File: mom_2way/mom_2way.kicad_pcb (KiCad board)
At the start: 2 copper layers, 15 x 17 mm, 9 parts, among them J1 I/O connector

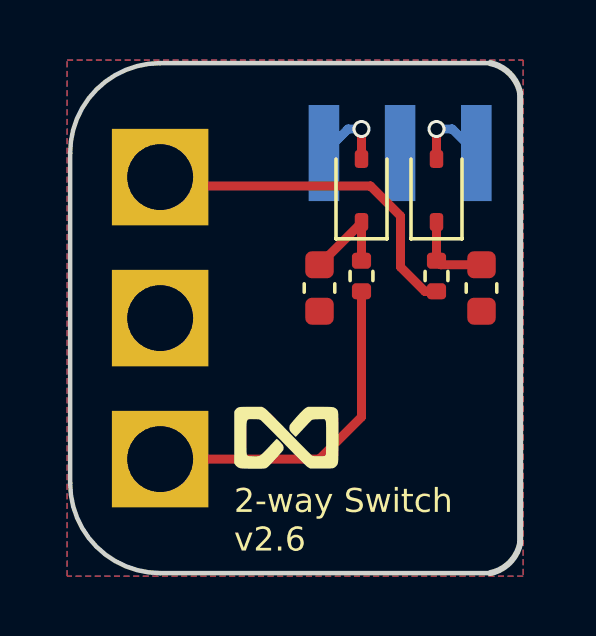
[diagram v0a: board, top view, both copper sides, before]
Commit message: 2-Way Switch refinements
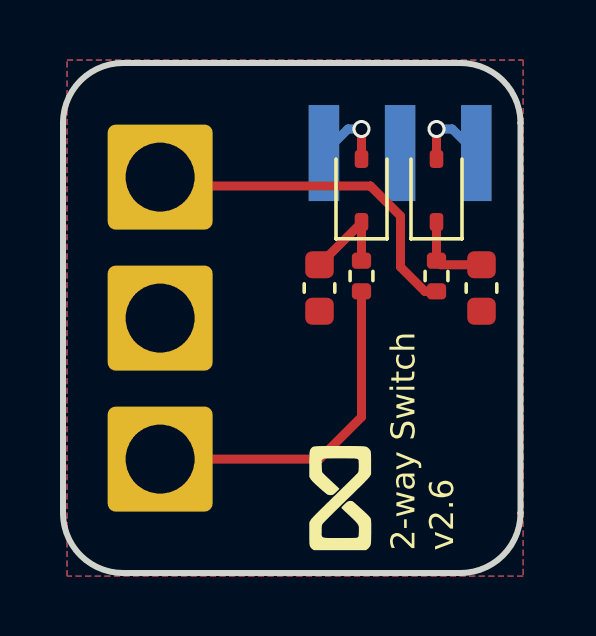
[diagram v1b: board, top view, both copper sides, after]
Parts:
- moved G*** 2.69 mm to (150.0, 111.0), turned to 90 degrees
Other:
- board size 15 x 17 mm -> 15.2 x 17 mm
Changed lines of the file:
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@@
 		(sheetname "/")
 		(sheetfile "mom_2way.kicad_sch")
-		(pad "1" thru_hole rect
+		(pad "1" thru_hole roundrect
 			(at -4.7 0 270)
-			(size 3.216 3.216)
-			(drill 2.2)
+			(size 3.5 3.5)
+			(drill 2.3)
 			(layers "*.Cu" "*.Mask")
 			(remove_unused_layers no)
+			(roundrect_rratio 0.07692307692)
 			(net 5 "Net-(S1-O)")
 			(pinfunction "O")
@@
 			(thermal_bridge_angle 0)
 		)
-		(pad "2" thru_hole rect
+		(pad "2" thru_hole roundrect
 			(at 0 0 270)
-			(size 3.216 3.216)
-			(drill 2.2)
+			(size 3.5 3.5)
+			(drill 2.3)
 			(layers "*.Cu" "*.Mask")
 			(remove_unused_layers no)
+			(roundrect_rratio 0.07692307692)
 			(net 1 "GND")
 			(pinfunction "P")
@@
 			(thermal_bridge_angle 0)
 		)
-		(pad "3" thru_hole rect
+		(pad "3" thru_hole roundrect
 			(at 4.7 0 270)
-			(size 3.216 3.216)
-			(drill 2.2)
+			(size 3.5 3.5)
+			(drill 2.3)
 			(layers "*.Cu" "*.Mask")
 			(remove_unused_layers no)
+			(roundrect_rratio 0.07692307692)
 			(net 4 "Net-(S1-S)")
 			(pinfunction "S")
@@
 		)
 		(embedded_fonts no)
+		(model "${CYCFI_COMMON}/step_files/141_100SPxT1B1M1xE.stp"
+			(offset
+				(xyz 0 0 7)
+			)
+			(scale
+				(xyz 1 1 1)
+			)
+			(rotate
+				(xyz -0 -0 -0)
+			)
+		)
 	)
 	(footprint "cycfi_library:infinity_logo_4mm"
 		(layer "F.Cu")
-		(at 148.2 109)
+		(at 150 111 90)
 		(property "Reference" "G***"
-			(at 0 0 0)
+			(at 0 0 90)
 			(layer "F.SilkS")
 			(hide yes)
@@
 		)
 		(property "Value" "LOGO"
-			(at 0.75 0 0)
+			(at 0.75 0 90)
 			(layer "F.SilkS")
 			(hide yes)
@@
 		)
 		(property "Datasheet" ""
-			(at 0 0 0)
+			(at 0 0 90)
 			(layer "F.Fab")
 			(hide yes)
@@
 		)
 		(property "Description" ""
-			(at 0 0 0)
+			(at 0 0 90)
 			(layer "F.Fab")
 			(hide yes)
@@
 	)
 	(gr_line
-		(start 154.9878 96.503599)
-		(end 143.9878 96.503599)
-		(stroke
-			(width 0.15)
-			(type solid)
+		(start 140.75 111.5)
+		(end 140.75 98.5)
+		(stroke
+			(width 0.2)
+			(type default)
 		)
 		(layer "Edge.Cuts")
 	)
 	(gr_line
-		(start 143.9878 113.503599)
-		(end 154.9878 113.503599)
-		(stroke
-			(width 0.15)
-			(type solid)
+		(start 156 98.5)
+		(end 156 111.5)
+		(stroke
+			(width 0.2)
+			(type default)
+		)
+		(layer "Edge.Cuts")
+	)
+	(gr_arc
+		(start 154 96.5)
+		(mid 155.414214 97.085786)
+		(end 156 98.5)
+		(stroke
+			(width 0.2)
+			(type default)
 		)
 		(layer "Edge.Cuts")
 	)
 	(gr_line
-		(start 155.9878 97.503599)
-		(end 155.9878 112.503599)
-		(stroke
-			(width 0.2032)
-			(type solid)
+		(start 142.75 96.5)
+		(end 154 96.5)
+		(stroke
+			(width 0.2)
+			(type default)
+		)
+		(layer "Edge.Cuts")
+	)
+	(gr_line
+		(start 154 113.5)
+		(end 142.75 113.5)
+		(stroke
+			(width 0.2)
+			(type default)
 		)
 		(layer "Edge.Cuts")
 	)
 	(gr_arc
-		(start 143.9878 113.503599)
-		(mid 141.86648 112.624919)
-		(end 140.9878 110.503599)
-		(stroke
-			(width 0.15)
-			(type solid)
+		(start 140.75 98.5)
+		(mid 141.335786 97.085786)
+		(end 142.75 96.5)
+		(stroke
+			(width 0.2)
+			(type default)
 		)
 		(layer "Edge.Cuts")
 	)
 	(gr_arc
-		(start 140.9878 99.503599)
-		(mid 141.86648 97.382279)
-		(end 143.9878 96.503599)
-		(stroke
-			(width 0.15)
-			(type solid)
+		(start 156 111.5)
+		(mid 155.414214 112.914214)
+		(end 154 113.5)
+		(stroke
+			(width 0.2)
+			(type default)
 		)
 		(layer "Edge.Cuts")
 	)
 	(gr_arc
-		(start 155.9878 112.503599)
-		(mid 155.639188 113.154988)
-		(end 154.987799 113.5036)
-		(stroke
-			(width 0.2032)
-			(type solid)
-		)
-		(layer "Edge.Cuts")
-	)
-	(gr_arc
-		(start 154.9878 96.503599)
-		(mid 155.639188 96.852212)
-		(end 155.9878 97.503601)
-		(stroke
-			(width 0.2032)
-			(type solid)
-		)
-		(layer "Edge.Cuts")
-	)
-	(gr_line
-		(start 140.9878 99.503599)
-		(end 140.9878 110.503599)
-		(stroke
-			(width 0.15)
-			(type solid)
+		(start 142.75 113.5)
+		(mid 141.335786 112.914214)
+		(end 140.75 111.5)
+		(stroke
+			(width 0.2)
+			(type default)
 		)
 		(layer "Edge.Cuts")
 	)
 	(gr_text "2-way Switch \nv2.6"
-		(at 146.45 112.85 0)
+		(at 153.85 112.75 90)
 		(layer "F.SilkS")
 		(effects

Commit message: Cleanup and refinements
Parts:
- turned C2 to 90 degrees
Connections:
- C2 pad 1: Net-(D2-K) -> GND
- C2 pad 2: GND -> Net-(D2-K)
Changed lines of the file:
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@@
 	(footprint "Capacitor_SMD:C_0603_1608Metric"
 		(layer "F.Cu")
-		(at 149.3 104 -90)
+		(at 149.3 104 90)
 		(descr "Capacitor SMD 0603 (1608 Metric), square (rectangular) end terminal, IPC-7351 nominal, (Body size source: IPC-SM-782 page 76, https://www.pcb-3d.com/wordpress/wp-content/uploads/ipc-sm-782a_amendment_1_and_2.pdf), generated with kicad-footprint-generator")
 		(tags "capacitor")
@@
 		)
 		(property "LCSC" "C15849"
-			(at 0 0 270)
+			(at 0 0 90)
 			(unlocked yes)
 			(layer "F.Fab")
@@
 		(attr smd)
 		(fp_line
+			(start -0.14058 -0.51)
+			(end 0.14058 -0.51)
+			(stroke
+				(width 0.12)
+				(type solid)
+			)
+			(layer "F.SilkS")
+		)
+		(fp_line
 			(start -0.14058 0.51)
 			(end 0.14058 0.51)
@@
 		)
 		(fp_line
-			(start -0.14058 -0.51)
-			(end 0.14058 -0.51)
+			(start 1.48 -0.73)
+			(end 1.48 0.73)
 			(stroke
-				(width 0.12)
+				(width 0.05)
 				(type solid)
 			)
-			(layer "F.SilkS")
+			(layer "F.CrtYd")
 		)
 		(fp_line
-			(start -1.48 0.73)
-			(end -1.48 -0.73)
+			(start -1.48 -0.73)
+			(end 1.48 -0.73)
 			(stroke
 				(width 0.05)
@@
 		)
 		(fp_line
-			(start -1.48 -0.73)
-			(end 1.48 -0.73)
+			(start -1.48 0.73)
+			(end -1.48 -0.73)
 			(stroke
 				(width 0.05)
@@
 		)
 		(fp_line
-			(start 1.48 -0.73)
-			(end 1.48 0.73)
+			(start 0.8 -0.4)
+			(end 0.8 0.4)
 			(stroke
-				(width 0.05)
+				(width 0.1)
 				(type solid)
 			)
-			(layer "F.CrtYd")
+			(layer "F.Fab")
 		)
 		(fp_line
-			(start -0.8 0.4)
-			(end -0.8 -0.4)
+			(start -0.8 -0.4)
+			(end 0.8 -0.4)
 			(stroke
 				(width 0.1)
@@
 		)
 		(fp_line
-			(start -0.8 -0.4)
-			(end 0.8 -0.4)
-			(stroke
-				(width 0.1)
-				(type solid)
-			)
-			(layer "F.Fab")
-		)
-		(fp_line
-			(start 0.8 -0.4)
-			(end 0.8 0.4)
+			(start -0.8 0.4)
+			(end -0.8 -0.4)
 			(stroke
 				(width 0.1)
@@
 		)
 		(pad "1" smd roundrect
-			(at -0.775 0 270)
+			(at -0.775 0 90)
+			(size 0.9 0.95)
+			(layers "F.Cu" "F.Mask" "F.Paste")
+			(roundrect_rratio 0.25)
+			(net 1 "GND")
+			(pintype "passive")
+		)
+		(pad "2" smd roundrect
+			(at 0.775 0 90)
 			(size 0.9 0.95)
 			(layers "F.Cu" "F.Mask" "F.Paste")
@@
 			(pintype "passive")
 		)
-		(pad "2" smd roundrect
-			(at 0.775 0 270)
-			(size 0.9 0.95)
-			(layers "F.Cu" "F.Mask" "F.Paste")
-			(roundrect_rratio 0.25)
-			(net 1 "GND")
-			(pintype "passive")
-		)
